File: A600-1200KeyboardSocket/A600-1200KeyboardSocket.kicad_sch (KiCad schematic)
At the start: 2 parts, among them J1 KBD, U1 68HC711_PLCC

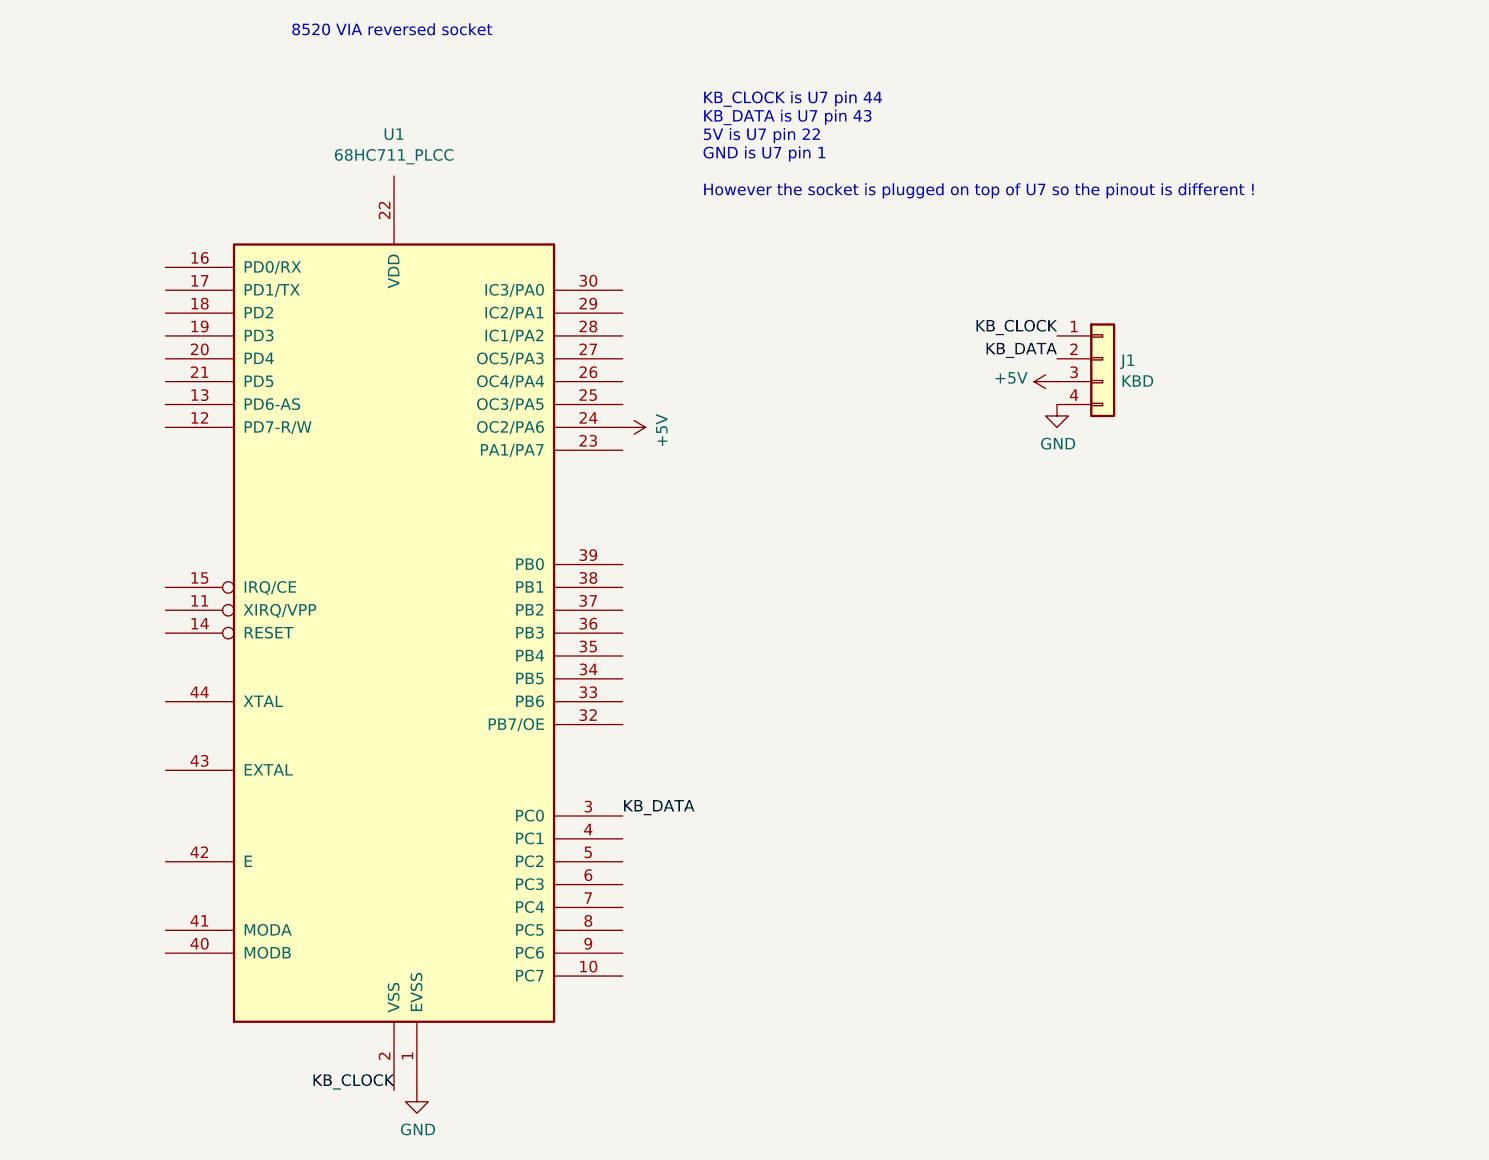
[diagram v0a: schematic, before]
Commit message: A600-1200KeyboardSocket : better symbol for PLCC socket
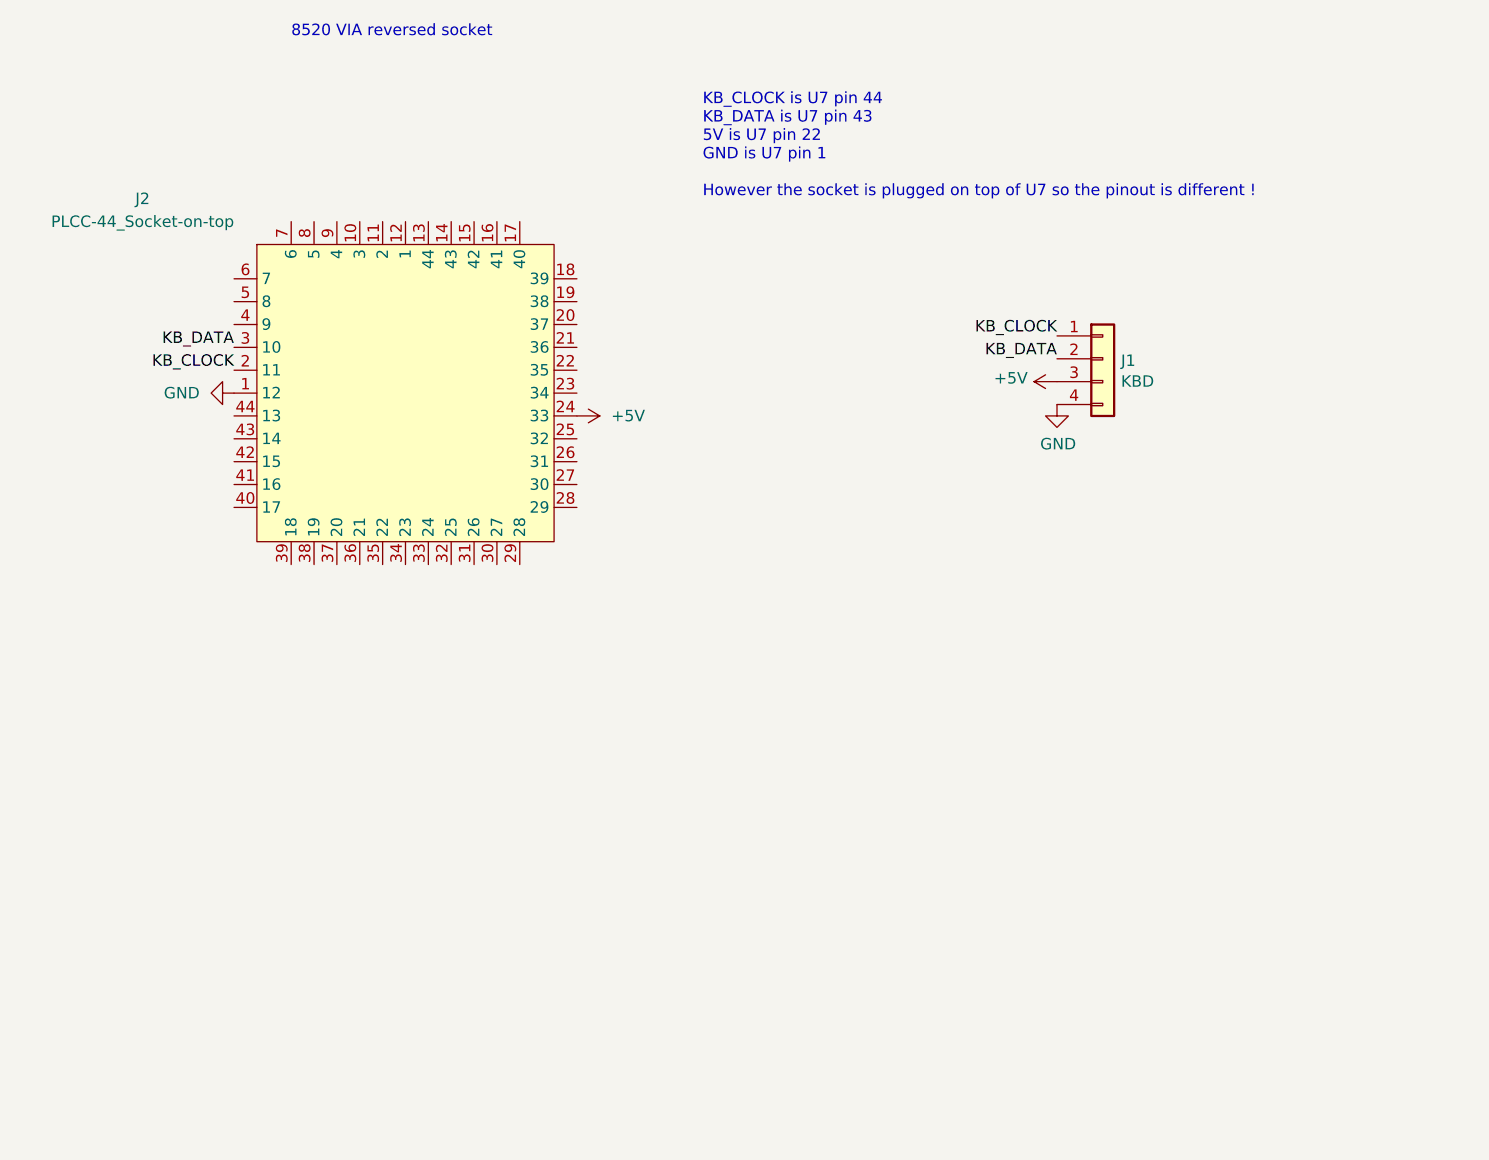
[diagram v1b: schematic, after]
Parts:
- removed U1: 68HC711_PLCC, Package_LCC:PLCC-44_THT-Socket, symbol MCU_NXP_HC11:68HC711_PLCC
- added J2: PLCC-44_Socket-on-top, Package_LCC:PLCC-44_THT-Socket, symbol Sassa:PLCC-44_Socket-on-top
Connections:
- net +5V: now also J2.24 (33)
- net GND: now also J2.1 (12)
- net KB_CLOCK: now also J2.2 (11)
- net KB_DATA: now also J2.3 (10)
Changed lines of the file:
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@@
     (effects (font (size 1.27 1.27)) (justify right bottom))
   )
-  (label "KB_CLOCK" (at 91.44 154.94 180)
+  (label "KB_CLOCK" (at 73.66 74.93 180)
     (effects (font (size 1.27 1.27)) (justify right bottom))
   )
@@
     (effects (font (size 1.27 1.27)) (justify right bottom))
   )
-  (label "KB_DATA" (at 116.84 124.46 0)
-    (effects (font (size 1.27 1.27)) (justify left bottom))
-  )
-  (symbol (lib_id "MCU_NXP_HC11:68HC711_PLCC") (at 91.44 104.14 0) (unit 1)
-    (in_bom yes) (on_board yes)
-    (property "Reference" "U1" (id 0) (at 91.44 48.7426 0))
-    (property "Value" "68HC711_PLCC" (id 1) (at 91.44 51.054 0))
-    (property "Footprint" "Package_LCC:PLCC-44_THT-Socket" (id 2) (at 91.44 104.14 0)
-      (effects (font (size 1.27 1.27)) hide)
-    )
-    (property "Datasheet" "" (id 3) (at 91.44 104.14 0)
-      (effects (font (size 1.27 1.27)) hide)
-    )
-    (pin "1")
-    (pin "10")
-    (pin "11")
-    (pin "12")
-    (pin "13")
-    (pin "14")
-    (pin "15")
-    (pin "16")
-    (pin "17")
-    (pin "18")
-    (pin "19")
-    (pin "2")
-    (pin "20")
-    (pin "21")
-    (pin "22")
-    (pin "23")
-    (pin "24")
-    (pin "25")
-    (pin "26")
-    (pin "27")
-    (pin "28")
-    (pin "29")
-    (pin "3")
-    (pin "30")
-    (pin "32")
-    (pin "33")
-    (pin "34")
-    (pin "35")
-    (pin "36")
-    (pin "37")
-    (pin "38")
-    (pin "39")
-    (pin "4")
-    (pin "40")
-    (pin "41")
-    (pin "42")
-    (pin "43")
-    (pin "44")
-    (pin "5")
-    (pin "6")
-    (pin "7")
-    (pin "8")
-    (pin "9")
+  (label "KB_DATA" (at 73.66 72.39 180)
+    (effects (font (size 1.27 1.27)) (justify right bottom))
   )
   (symbol (lib_id "Connector_Generic:Conn_01x04") (at 170.18 73.66 0) (unit 1)
@@
     (pin "1")
   )
-  (symbol (lib_id "power:GND") (at 93.98 154.94 0) (unit 1)
+  (symbol (lib_id "Sassa:PLCC-44_Socket-on-top") (at 92.71 77.47 0) (unit 1)
     (in_bom yes) (on_board yes)
-    (property "Reference" "#PWR02" (id 0) (at 93.98 161.29 0)
+    (property "Reference" "J2" (id 0) (at 63.5 55.88 0))
+    (property "Value" "PLCC-44_Socket-on-top" (id 1) (at 63.5 58.42 0))
+    (property "Footprint" "Package_LCC:PLCC-44_THT-Socket" (id 2) (at 92.71 77.47 0)
       (effects (font (size 1.27 1.27)) hide)
     )
-    (property "Value" "GND" (id 1) (at 94.107 159.3342 0))
-    (property "Footprint" "" (id 2) (at 93.98 154.94 0)
+    (property "Datasheet" "" (id 3) (at 92.71 77.47 0)
       (effects (font (size 1.27 1.27)) hide)
     )
-    (property "Datasheet" "" (id 3) (at 93.98 154.94 0)
+    (pin "1")
+    (pin "10")
+    (pin "11")
+    (pin "12")
+    (pin "13")
+    (pin "14")
+    (pin "15")
+    (pin "16")
+    (pin "17")
+    (pin "18")
+    (pin "19")
+    (pin "2")
+    (pin "20")
+    (pin "21")
+    (pin "22")
+    (pin "23")
+    (pin "24")
+    (pin "25")
+    (pin "26")
+    (pin "27")
+    (pin "28")
+    (pin "29")
+    (pin "3")
+    (pin "30")
+    (pin "31")
+    (pin "32")
+    (pin "33")
+    (pin "34")
+    (pin "35")
+    (pin "36")
+    (pin "37")
+    (pin "38")
+    (pin "39")
+    (pin "4")
+    (pin "40")
+    (pin "41")
+    (pin "42")
+    (pin "43")
+    (pin "44")
+    (pin "5")
+    (pin "6")
+    (pin "7")
+    (pin "8")
+    (pin "9")
+  )
+  (symbol (lib_id "power:GND") (at 73.66 77.47 270) (unit 1)
+    (in_bom yes) (on_board yes) (fields_autoplaced)
+    (property "Reference" "#PWR01" (id 0) (at 67.31 77.47 0)
+      (effects (font (size 1.27 1.27)) hide)
+    )
+    (property "Value" "GND" (id 1) (at 69.85 77.4699 90)
+      (effects (font (size 1.27 1.27)) (justify right))
+    )
+    (property "Footprint" "" (id 2) (at 73.66 77.47 0)
+      (effects (font (size 1.27 1.27)) hide)
+    )
+    (property "Datasheet" "" (id 3) (at 73.66 77.47 0)
       (effects (font (size 1.27 1.27)) hide)
     )
     (pin "1")
   )
-  (symbol (lib_id "power:+5V") (at 116.84 81.28 270) (unit 1)
-    (in_bom yes) (on_board yes)
-    (property "Reference" "#PWR01" (id 0) (at 113.03 81.28 0)
+  (symbol (lib_id "power:+5V") (at 111.76 80.01 270) (unit 1)
+    (in_bom yes) (on_board yes) (fields_autoplaced)
+    (property "Reference" "#PWR02" (id 0) (at 107.95 80.01 0)
       (effects (font (size 1.27 1.27)) hide)
     )
-    (property "Value" "+5V" (id 1) (at 121.2342 81.661 0))
-    (property "Footprint" "" (id 2) (at 116.84 81.28 0)
+    (property "Value" "+5V" (id 1) (at 115.57 80.0099 90)
+      (effects (font (size 1.27 1.27)) (justify left))
+    )
+    (property "Footprint" "" (id 2) (at 111.76 80.01 0)
       (effects (font (size 1.27 1.27)) hide)
     )
-    (property "Datasheet" "" (id 3) (at 116.84 81.28 0)
+    (property "Datasheet" "" (id 3) (at 111.76 80.01 0)
       (effects (font (size 1.27 1.27)) hide)
     )
@@
   )
   (symbol_instances
-    (path "/00000000-0000-0000-0000-00005f6538b2"
-      (reference "#PWR01") (unit 1) (value "+5V") (footprint "")
+    (path "/ad0880dc-b2e1-4bd9-bff8-eb61fb5f4960"
+      (reference "#PWR01") (unit 1) (value "GND") (footprint "")
     )
-    (path "/00000000-0000-0000-0000-00005f652808"
-      (reference "#PWR02") (unit 1) (value "GND") (footprint "")
+    (path "/f1022dde-4b98-4487-ac15-9696f45187f2"
+      (reference "#PWR02") (unit 1) (value "+5V") (footprint "")
     )
     (path "/00000000-0000-0000-0000-00005f651cd6"
@@
       (reference "J1") (unit 1) (value "KBD") (footprint "Connector_PinHeader_2.54mm:PinHeader_1x04_P2.54mm_Vertical")
     )
-    (path "/00000000-0000-0000-0000-00005f650457"
-      (reference "U1") (unit 1) (value "68HC711_PLCC") (footprint "Package_LCC:PLCC-44_THT-Socket")
+    (path "/4d56bd2c-d7ae-4e71-a34c-7872a3891e14"
+      (reference "J2") (unit 1) (value "PLCC-44_Socket-on-top") (footprint "Package_LCC:PLCC-44_THT-Socket")
     )
   )

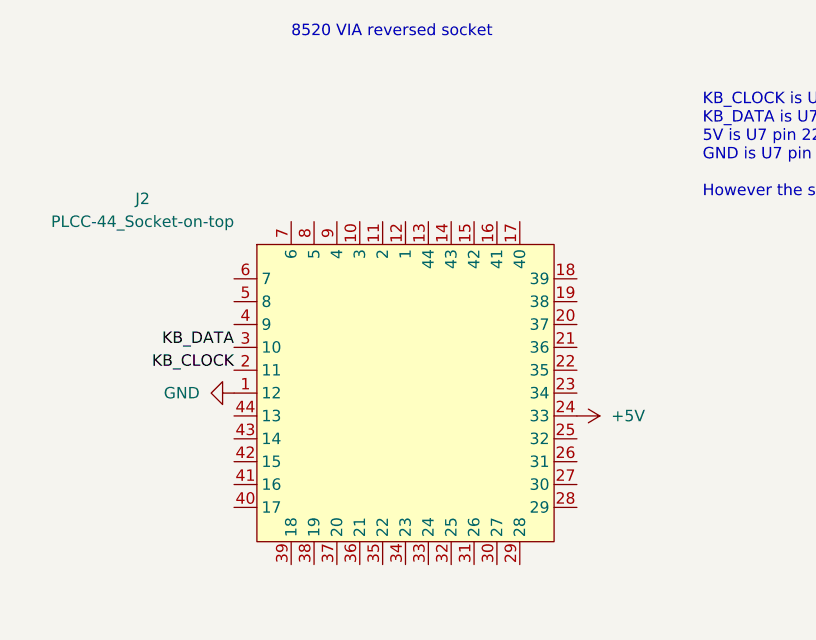
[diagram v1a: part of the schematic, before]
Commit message: A1200PcmciaResetFix, A600-1200KeyboardSocket : update socket symbol and footprint, no PCB change
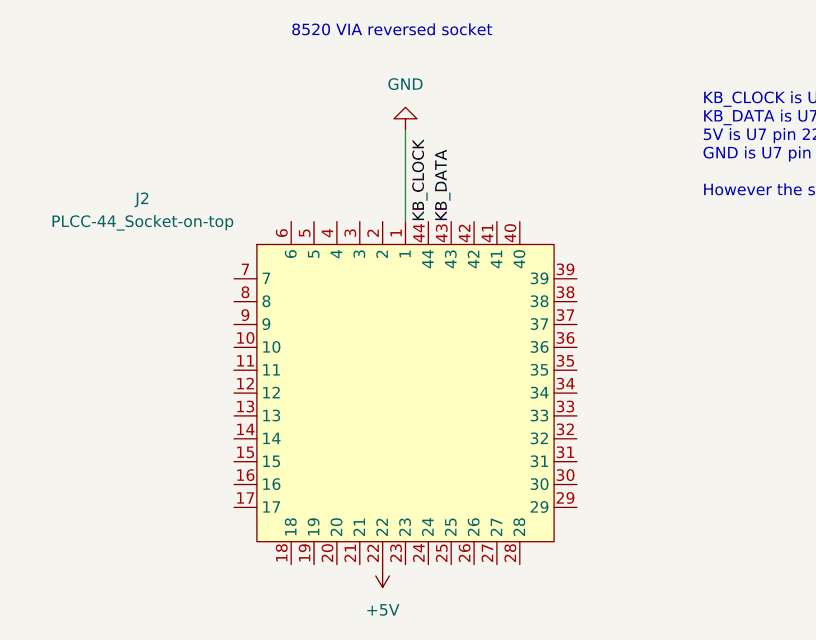
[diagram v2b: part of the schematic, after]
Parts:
- J2: footprint Package_LCC:PLCC-44_THT-Socket -> Sassa:PLCC-44_THT-SocketOnTop; symbol Sassa:PLCC-44_Socket-on-top -> Sassa:PLCC-44
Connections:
- net +5V: now also J2.22; no longer J2.24 (33)
- net KB_CLOCK: now also J2.44; no longer J2.2 (11)
- net KB_DATA: now also J2.43; no longer J2.3 (10)
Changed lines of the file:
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@@
     (company "FLACO 2020, licence of this schematic is CC-BY-NC-SA")
+  )
+  (wire (pts (xy 92.71 48.26) (xy 92.71 58.42))
+    (stroke (width 0) (type default) (color 0 0 0 0))
   )
   (text "KB_CLOCK is U7 pin 44\nKB_DATA is U7 pin 43\n5V is U7 pin 22\nGND is U7 pin 1\n\nHowever the socket is plugged on top of U7 so the pinout is different !"
@@
     (effects (font (size 1.27 1.27)) (justify right bottom))
   )
-  (label "KB_CLOCK" (at 73.66 74.93 180)
-    (effects (font (size 1.27 1.27)) (justify right bottom))
+  (label "KB_CLOCK" (at 95.25 58.42 90)
+    (effects (font (size 1.27 1.27)) (justify left bottom))
   )
   (label "KB_CLOCK" (at 165.1 71.12 180)
     (effects (font (size 1.27 1.27)) (justify right bottom))
   )
-  (label "KB_DATA" (at 73.66 72.39 180)
-    (effects (font (size 1.27 1.27)) (justify right bottom))
+  (label "KB_DATA" (at 97.79 58.42 90)
+    (effects (font (size 1.27 1.27)) (justify left bottom))
   )
   (symbol (lib_id "Connector_Generic:Conn_01x04") (at 170.18 73.66 0) (unit 1)
@@
     (pin "1")
   )
-  (symbol (lib_id "Sassa:PLCC-44_Socket-on-top") (at 92.71 77.47 0) (unit 1)
+  (symbol (lib_id "Sassa:PLCC-44") (at 92.71 77.47 0) (unit 1)
     (in_bom yes) (on_board yes)
     (property "Reference" "J2" (id 0) (at 63.5 55.88 0))
     (property "Value" "PLCC-44_Socket-on-top" (id 1) (at 63.5 58.42 0))
-    (property "Footprint" "Package_LCC:PLCC-44_THT-Socket" (id 2) (at 92.71 77.47 0)
+    (property "Footprint" "Sassa:PLCC-44_THT-SocketOnTop" (id 2) (at 92.71 77.47 0)
       (effects (font (size 1.27 1.27)) hide)
     )
@@
     (pin "9")
   )
-  (symbol (lib_id "power:GND") (at 73.66 77.47 270) (unit 1)
+  (symbol (lib_id "power:GND") (at 92.71 48.26 180) (unit 1)
     (in_bom yes) (on_board yes) (fields_autoplaced)
-    (property "Reference" "#PWR01" (id 0) (at 67.31 77.47 0)
+    (property "Reference" "#PWR01" (id 0) (at 92.71 41.91 0)
       (effects (font (size 1.27 1.27)) hide)
     )
-    (property "Value" "GND" (id 1) (at 69.85 77.4699 90)
-      (effects (font (size 1.27 1.27)) (justify right))
-    )
-    (property "Footprint" "" (id 2) (at 73.66 77.47 0)
+    (property "Value" "GND" (id 1) (at 92.71 43.18 0))
+    (property "Footprint" "" (id 2) (at 92.71 48.26 0)
       (effects (font (size 1.27 1.27)) hide)
     )
-    (property "Datasheet" "" (id 3) (at 73.66 77.47 0)
+    (property "Datasheet" "" (id 3) (at 92.71 48.26 0)
       (effects (font (size 1.27 1.27)) hide)
     )
     (pin "1")
   )
-  (symbol (lib_id "power:+5V") (at 111.76 80.01 270) (unit 1)
+  (symbol (lib_id "power:+5V") (at 90.17 96.52 180) (unit 1)
     (in_bom yes) (on_board yes) (fields_autoplaced)
-    (property "Reference" "#PWR02" (id 0) (at 107.95 80.01 0)
+    (property "Reference" "#PWR02" (id 0) (at 90.17 92.71 0)
       (effects (font (size 1.27 1.27)) hide)
     )
-    (property "Value" "+5V" (id 1) (at 115.57 80.0099 90)
-      (effects (font (size 1.27 1.27)) (justify left))
-    )
-    (property "Footprint" "" (id 2) (at 111.76 80.01 0)
+    (property "Value" "+5V" (id 1) (at 90.17 101.6 0))
+    (property "Footprint" "" (id 2) (at 90.17 96.52 0)
       (effects (font (size 1.27 1.27)) hide)
     )
-    (property "Datasheet" "" (id 3) (at 111.76 80.01 0)
+    (property "Datasheet" "" (id 3) (at 90.17 96.52 0)
       (effects (font (size 1.27 1.27)) hide)
     )
@@
     )
     (path "/4d56bd2c-d7ae-4e71-a34c-7872a3891e14"
-      (reference "J2") (unit 1) (value "PLCC-44_Socket-on-top") (footprint "Package_LCC:PLCC-44_THT-Socket")
+      (reference "J2") (unit 1) (value "PLCC-44_Socket-on-top") (footprint "Sassa:PLCC-44_THT-SocketOnTop")
     )
   )
